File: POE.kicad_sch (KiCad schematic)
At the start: 36 parts, among them J3 Conn_02x04_Odd_Even, Q1 FDS2582, Q2 FDS8880, T1 PA2369NL, T2 PE-68386NL, U3 LTC4269-1

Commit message: Routing changes, pullups, etc
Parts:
- removed J3: Conn_02x04_Odd_Even, Connector_PinHeader_2.54mm:PinHeader_2x04_P2.54mm_Vertical, symbol Connector_Generic:Conn_02x04_Odd_Even
- added J3, J5: 7466003R, hub75_poe:7466003R, symbol Connector:Screw_Terminal_01x01
- C10, C11, C12, C13, C20, C6, C7, C8, C9, D1, D11, D12, D2, D3, D4, D5, L1, Q1, Q2, R10, R11, R12, R2, R21, R22, R3, R4, R5, R6, R7, R8, R9, T1, T2, U3: Source (none) -> ANY
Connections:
- net GND: now also J5.1 (Pin_1)
- net VBUS: now also J3.1 (Pin_1)

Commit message: Routing cleanup, fix primary transformer
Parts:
- C13: value 470uf -> 470uf+
- L1: value L -> SRN6045TA-2R2Y; footprint Inductor_SMD:L_Bourns-SRN4018 -> Inductor_SMD:L_Bourns_SRN6045TA
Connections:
- net GNDPWR: now also T1.5; no longer T1.2
- net POE_P: now also T1.2; no longer T1.5
- net at D4.1 (A), R9.1: now also T1.3; no longer T1.1
- net at Q1.5 (D), Q1.6 (D), Q1.7 (D)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: now also T1.1; no longer T1.3
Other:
- moved on the sheet: C10, C11, C12, C13, C20, C6, C7, C8, C9, D1, D11, D12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

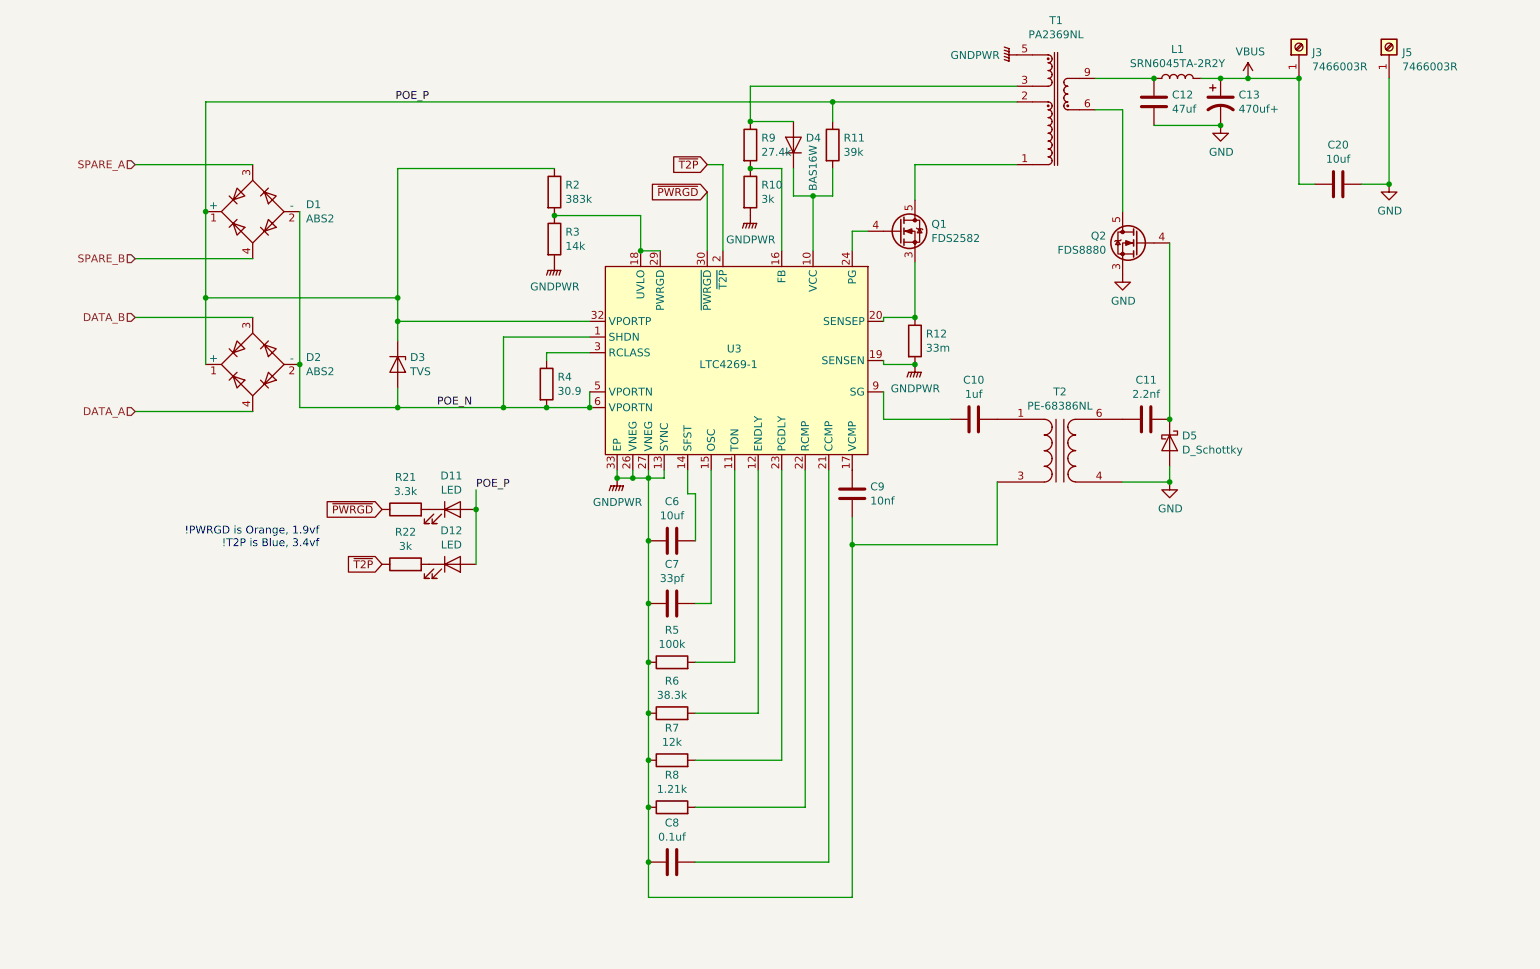
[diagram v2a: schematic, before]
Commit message: Change PoE controller to NCP1081
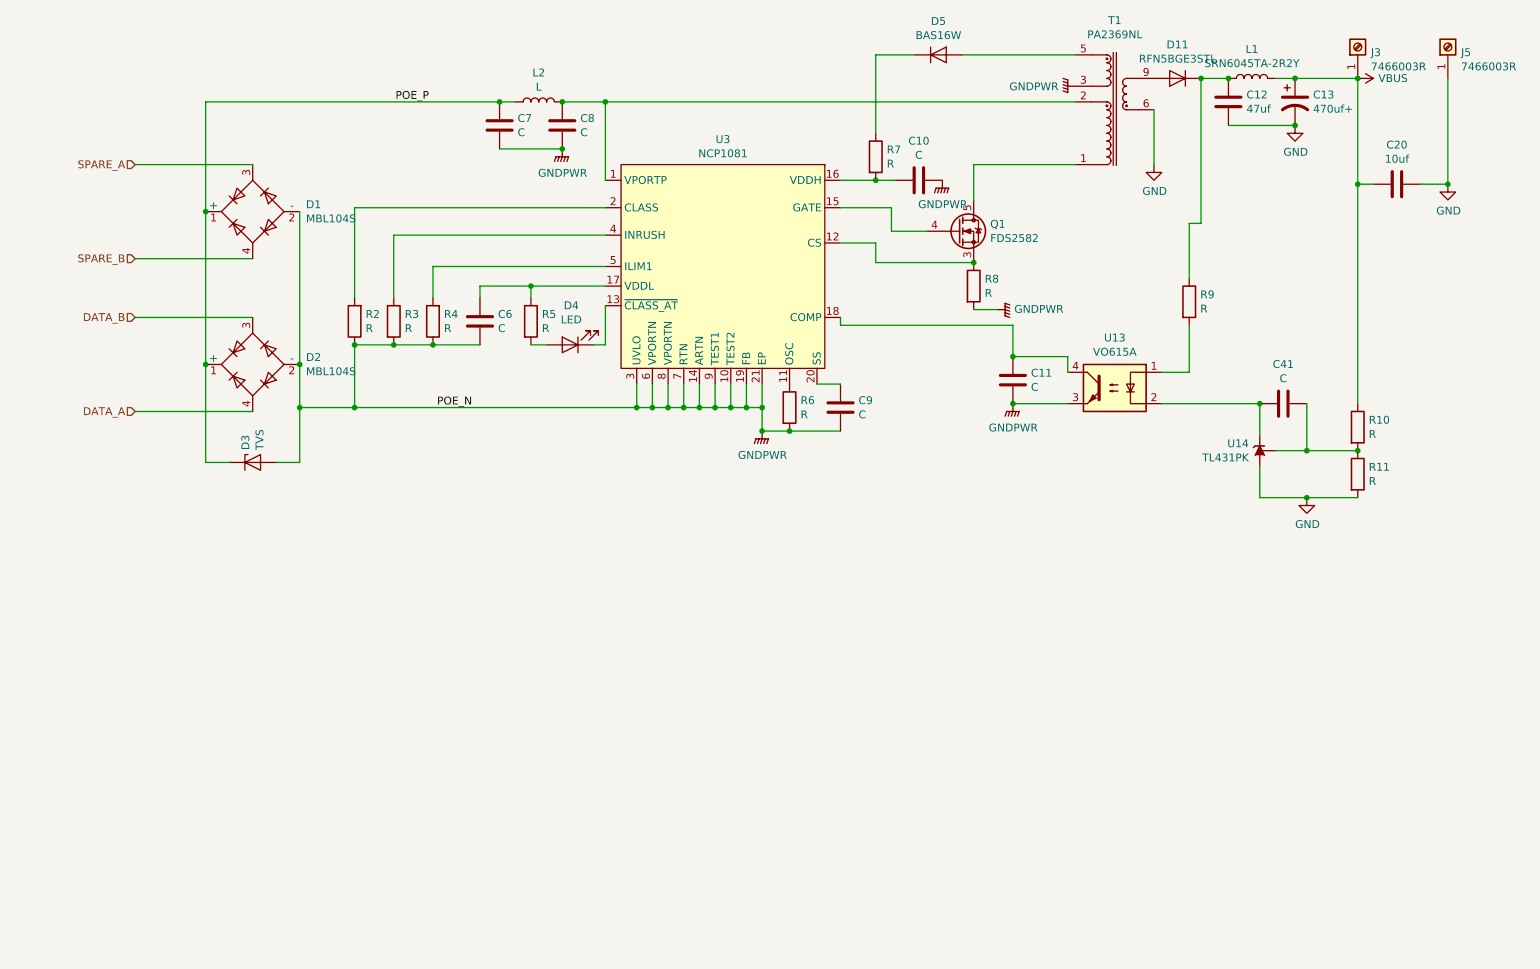
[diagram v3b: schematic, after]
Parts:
- removed D1, D2: ABS2, Diode_SMD:Diode_Bridge_Diotec_ABS, symbol Diode_Bridge:ABS2
- removed D11, D12: LED, Diode_SMD:D_0402_1005Metric, symbol Device:LED
- removed D4: BAS16W, Package_TO_SOT_SMD:SOT-323_SC-70, symbol Diode:BAS16W
- removed D5: D_Schottky, Diode_SMD:D_0805_2012Metric_Castellated, symbol Device:D_Schottky
- removed Q2: FDS8880, Package_SO:SOP-8_3.9x4.9mm_P1.27mm, symbol h75_poe:FDS8880
- removed R12: 33m, Resistor_SMD:R_2512_6332Metric, symbol Device:R
- removed R21: 3.3k, Resistor_SMD:R_0402_1005Metric, symbol Device:R
- removed R22: 3k, Resistor_SMD:R_0402_1005Metric, symbol Device:R
- removed T2: PE-68386NL, hub75_poe:PE-68386NL, symbol h75_poe:PE-68386NL
- removed U3: LTC4269-1, Package_DFN_QFN:DFN-32-1EP_4x7mm_P0.4mm_EP2.64x6.44mm, symbol h75_poe:LTC4269-1
- added C41: C, Capacitor_SMD:C_0402_1005Metric, symbol Device:C
- added D1, D2: MBL104S, Diode_SMD:Diode_Bridge_Vishay_MBLS, symbol Diode_Bridge:MBL104S
- added D11: RFN5BGE3STL, Package_TO_SOT_SMD:TO-252-2, symbol h75_poe:RFN5BGE3STL
- added D4: LED, Diode_SMD:D_0805_2012Metric_Castellated, symbol Device:LED
- added D5: BAS16W, Package_TO_SOT_SMD:SOT-323_SC-70, symbol Diode:BAS16W
- added L2: L, Inductor_SMD:L_Bourns-SRN8040_8x8.15mm, symbol Device:L
- added U13: VO615A, Package_SO:SO-4_4.4x3.9mm_P2.54mm, symbol Isolator:VO615A
- added U14: TL431PK, Package_TO_SOT_SMD:SOT-89-3, symbol Reference_Voltage:TL431PK
- added U3: NCP1081, Package_SO:HTSSOP-20-1EP_4.4x6.5mm_P0.65mm_EP3.4x6.5mm, symbol h75_poe:NCP1081
- C10: value 1uf -> C; footprint Capacitor_SMD:C_0805_2012Metric -> Capacitor_SMD:C_0402_1005Metric; Source ANY -> (none)
- C11: value 2.2nf -> C; footprint Capacitor_SMD:C_0805_2012Metric -> Capacitor_SMD:C_0402_1005Metric; Source ANY -> (none)
- C13: footprint Capacitor_SMD:CP_Elec_10x12.6 -> Capacitor_SMD:CP_Elec_8x10
- C6: value 10uf -> C; Source ANY -> (none)
- C7: value 33pf -> C; footprint Capacitor_SMD:C_0402_1005Metric -> Capacitor_SMD:C_1210_3225Metric; Source ANY -> (none)
- C8: value 0.1uf -> C; footprint Capacitor_SMD:C_0402_1005Metric -> Capacitor_SMD:C_1210_3225Metric; Source ANY -> (none)
- C9: value 10nf -> C; Source ANY -> (none)
- Q1: Source ANY -> (none)
- R10: value 3k -> R; Source ANY -> (none)
- R11: value 39k -> R; Source ANY -> (none)
- R2: value 383k -> R; Source ANY -> (none)
- R3: value 14k -> R; Source ANY -> (none)
- R4: value 30.9 -> R; footprint Resistor_SMD:R_0603_1608Metric -> Resistor_SMD:R_0402_1005Metric; Source ANY -> (none)
- R5: value 100k -> R; Source ANY -> (none)
- R6: value 38.3k -> R; Source ANY -> (none)
- R7: value 12k -> R; Source ANY -> (none)
- R8: value 1.21k -> R; footprint Resistor_SMD:R_0402_1005Metric -> Resistor_SMD:R_2512_6332Metric; Source ANY -> (none)
- R9: value 27.4k -> R; Source ANY -> (none)
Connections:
- net DATA_A: now also D2.4 (~~)
- net DATA_B: now also D2.3 (~~)
- net GND: now also R11.2, T1.6, T1.7, U14.2 (A)
- net GNDPWR: now also C10.2, C11.2, C6.2, C7.2, C8.2, D3.2 (A2), R2.1, R4.1, R6.2, R8.2, T1.3, D1.2 (-), D2.2 (-), U13.3, U3.10 (TEST2), U3.14 (ARTN), U3.19 (FB), U3.21 (EP), U3.3 (UVLO), U3.6 (VPORTN), U3.7 (RTN), U3.8 (VPORTN), U3.9 (TEST1); no longer C6.1, C7.1, C8.1, R10.2, R5.1, R6.1, R7.1, R8.1, T1.5
- net POE_P: now also C7.1, D1.1 (+), D2.1 (+), L2.1; no longer R11.1, R2.1, T1.2
- net SPARE_A: now also D1.3 (~~)
- net SPARE_B: now also D1.4 (~~)
- net VBUS: now also R10.1
- net at R9.1: now also C12.1, L1.1, D11.2 (K); no longer T1.3
- net at R9.2: now also U13.1; no longer R10.1
- net at Q1.1 (S), Q1.2 (S), Q1.3 (S): now also R8.1, U3.12 (CS)
- net at R5.2: now also D4.2 (A)
- net at R7.2: now also C10.1, U3.16 (VDDH)
- net at C9.1: now also U3.20 (SS)
- net at R2.2: now also U3.2 (CLASS); no longer R3.1
- net at Q1.4 (G): now also U3.15 (GATE)
- net at C11.1: now also U13.4, U3.18 (COMP)
- net at T1.10, T1.9: now also D11.1 (A), D11.3 (A); no longer C12.1, L1.1
- net POE_N: no longer names the net of R4.2
- net POE_N: now also U3.5 (ILIM1); no longer D3.2 (A2)
- new net: C41.2, R10.2, R11.1, U14.1 (REF)
- new net: D5.3 (K), R7.1
- new net: C41.1, U13.2, U14.3 (K)
- new net: R6.1, U3.11 (OSC)
- new net: C6.1, R5.1, U3.17 (VDDL)
- new net: D4.1 (K), U3.13 (~CLASS_AT)
- new net: R3.1, U3.4 (INRUSH)
- new net: D5.1 (A), T1.5
- new net: C8.1, L2.2, T1.2, U3.1 (VPORTP)
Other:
- note removed: "!PWRGD is Orange, 1.9vf !T2P is Blue, 3.4vf"
- moved on the sheet: C12, C13, C20, D3, J3, J5, L1, T1

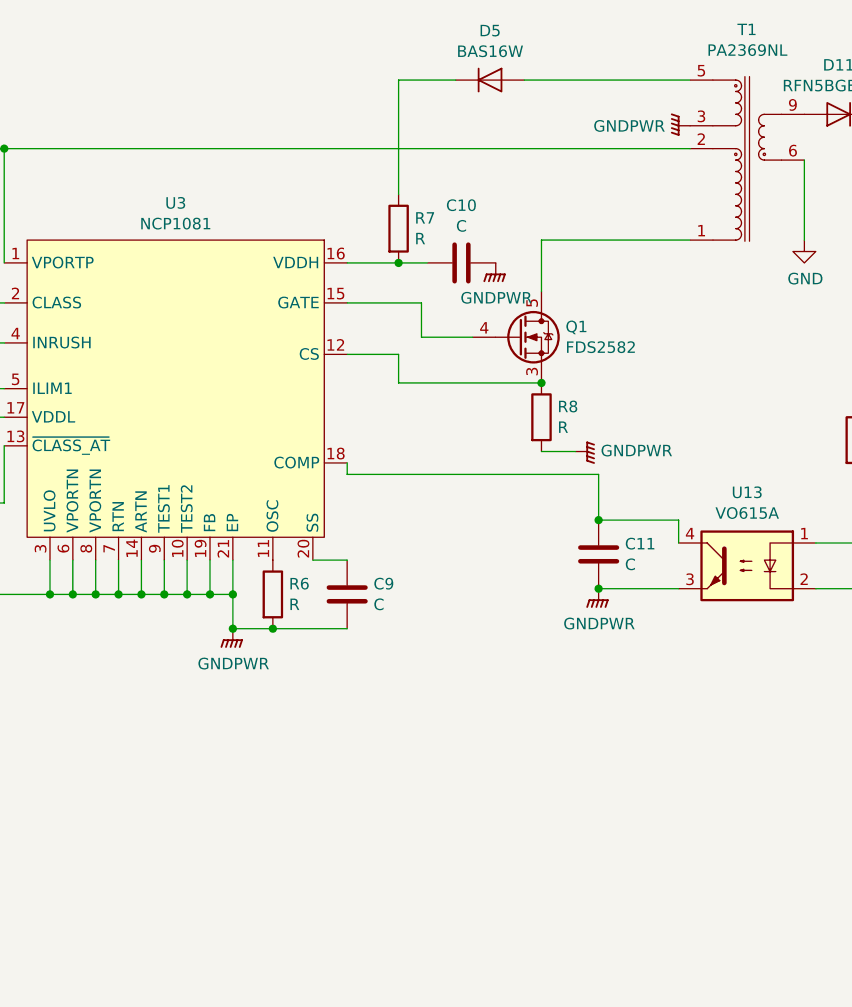
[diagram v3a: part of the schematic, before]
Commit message: Update routing and icons/text
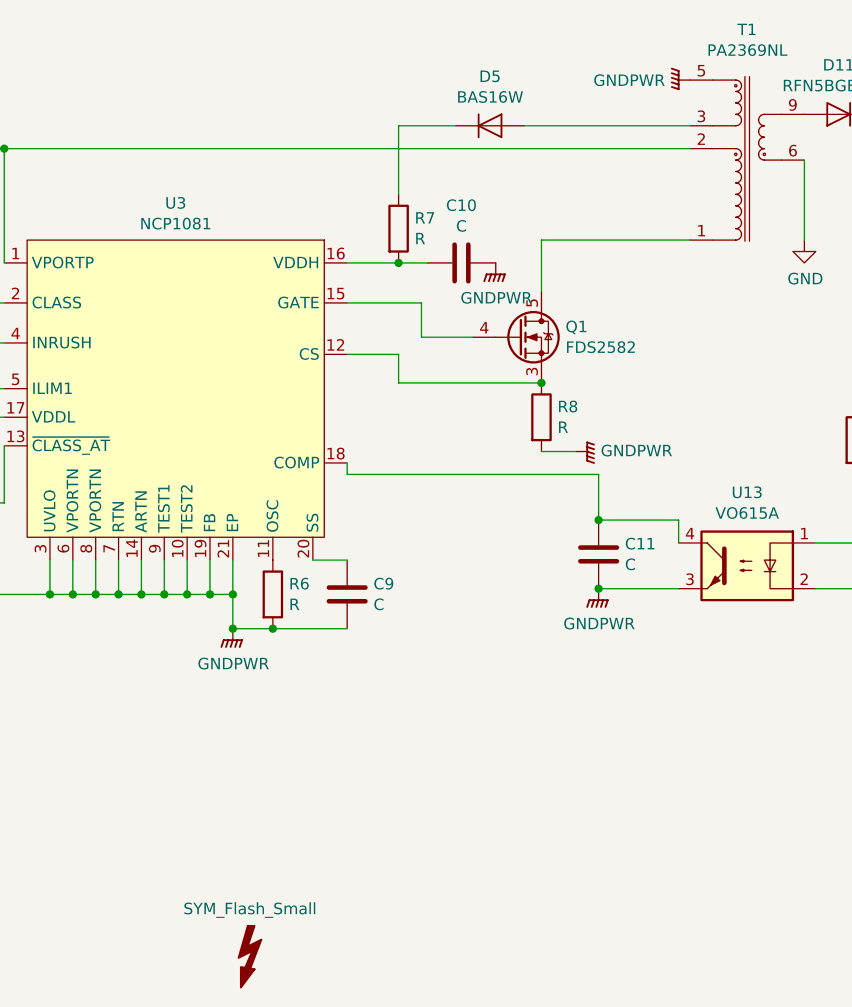
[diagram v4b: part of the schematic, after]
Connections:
- net GNDPWR: now also T1.5; no longer T1.3
- net at D5.1 (A): now also T1.3; no longer T1.5
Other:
- moved on the sheet: D5
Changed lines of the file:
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@@
-(kicad_sch (version 20200608) (host eeschema "5.99.0-unknown-8bd9b26~101~ubuntu20.04.1")
+(kicad_sch (version 20200608) (host eeschema "5.99.0-unknown-60915fb~101~ubuntu20.04.1")
   (page 4 7)
   (paper "A4")
@@
     (stroke (width 0) (type solid) (color 0 0 0 0))
   )
-  (wire (pts (xy 160.655 36.195) (xy 160.655 48.895))
+  (wire (pts (xy 160.655 41.275) (xy 160.655 48.895))
     (stroke (width 0) (type solid) (color 0 0 0 0))
   )
@@
     (stroke (width 0) (type solid) (color 0 0 0 0))
   )
-  (wire (pts (xy 167.005 36.195) (xy 160.655 36.195))
-    (stroke (width 0) (type solid) (color 0 0 0 0))
-  )
-  (wire (pts (xy 174.625 36.195) (xy 193.04 36.195))
+  (wire (pts (xy 167.005 41.275) (xy 160.655 41.275))
+    (stroke (width 0) (type solid) (color 0 0 0 0))
+  )
+  (wire (pts (xy 174.625 41.275) (xy 193.04 41.275))
     (stroke (width 0) (type solid) (color 0 0 0 0))
   )
@@
     )
   )
-  (symbol (lib_id "power:GNDPWR") (at 193.04 41.275 270) (unit 1)
-    (in_bom yes) (on_board yes)
-    (property "Reference" "#PWR0114" (id 0) (at 187.96 41.275 0)
-      (effects (font (size 1.27 1.27)) hide)
-    )
-    (property "Value" "GNDPWR" (id 1) (at 190.2714 41.3385 90)
-      (effects (font (size 1.27 1.27)) (justify right))
-    )
-    (property "Footprint" "" (id 2) (at 191.77 41.275 0)
-      (effects (font (size 1.27 1.27)) hide)
-    )
-    (property "Datasheet" "" (id 3) (at 191.77 41.275 0)
+  (symbol (lib_id "power:GNDPWR") (at 193.04 36.195 270) (unit 1)
+    (in_bom yes) (on_board yes)
+    (property "Reference" "#PWR0114" (id 0) (at 187.96 36.195 0)
+      (effects (font (size 1.27 1.27)) hide)
+    )
+    (property "Value" "GNDPWR" (id 1) (at 190.2714 36.2585 90)
+      (effects (font (size 1.27 1.27)) (justify right))
+    )
+    (property "Footprint" "" (id 2) (at 191.77 36.195 0)
+      (effects (font (size 1.27 1.27)) hide)
+    )
+    (property "Datasheet" "" (id 3) (at 191.77 36.195 0)
       (effects (font (size 1.27 1.27)) hide)
     )
@@
     )
   )
+  (symbol (lib_id "Graphic:SYM_Flash_Small") (at 144.145 133.985 0) (unit 1)
+    (in_bom yes) (on_board yes)
+    (property "Reference" "#SYM1" (id 0) (at 141.859 133.985 90)
+      (effects (font (size 1.27 1.27)) hide)
+    )
+    (property "Value" "SYM_Flash_Small" (id 1) (at 144.145 128.289 0))
+    (property "Footprint" "Symbol:Symbol_Highvoltage_Type1_CopperTop_Small" (id 2) (at 144.145 134.62 0)
+      (effects (font (size 1.27 1.27)) hide)
+    )
+    (property "Datasheet" "~" (id 3) (at 154.305 136.525 0)
+      (effects (font (size 1.27 1.27)) hide)
+    )
+  )
   (symbol (lib_id "Connector:Screw_Terminal_01x01") (at 238.76 34.925 90) (unit 1)
     (in_bom yes) (on_board yes)
@@
     )
   )
-  (symbol (lib_id "Diode:BAS16W") (at 170.815 36.195 0) (unit 1)
-    (in_bom yes) (on_board yes)
-    (property "Reference" "D5" (id 0) (at 170.815 30.7402 0))
-    (property "Value" "BAS16W" (id 1) (at 170.815 33.0389 0))
-    (property "Footprint" "Package_TO_SOT_SMD:SOT-323_SC-70" (id 2) (at 170.815 40.64 0)
-      (effects (font (size 1.27 1.27)) hide)
-    )
-    (property "Datasheet" "https://assets.nexperia.com/documents/data-sheet/BAS16_SER.pdf" (id 3) (at 170.815 36.195 0)
-      (effects (font (size 1.27 1.27)) hide)
-    )
+  (symbol (lib_id "Diode:BAS16W") (at 170.815 41.275 0) (unit 1)
+    (in_bom yes) (on_board yes)
+    (property "Reference" "D5" (id 0) (at 170.815 35.8202 0))
+    (property "Value" "BAS16W" (id 1) (at 170.815 38.1189 0))
+    (property "Footprint" "Package_TO_SOT_SMD:SOT-323_SC-70" (id 2) (at 170.815 45.72 0)
+      (effects (font (size 1.27 1.27)) hide)
+    )
+    (property "Datasheet" "https://assets.nexperia.com/documents/data-sheet/BAS16_SER.pdf" (id 3) (at 170.815 41.275 0)
+      (effects (font (size 1.27 1.27)) hide)
+    )
